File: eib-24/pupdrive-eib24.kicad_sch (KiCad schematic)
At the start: 27 parts, among them J1 050702422

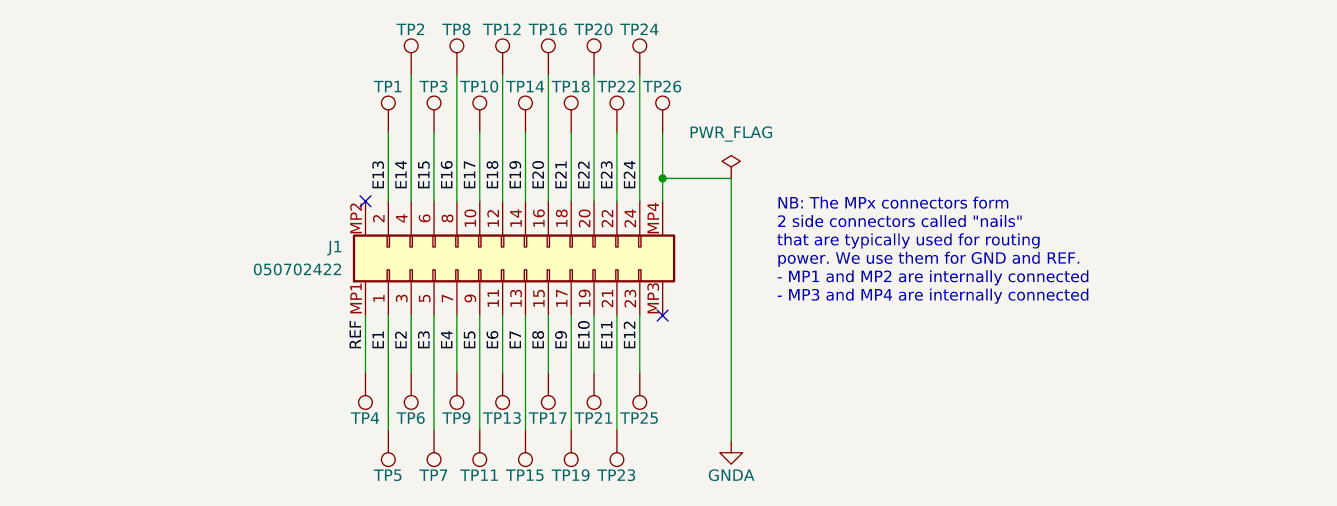
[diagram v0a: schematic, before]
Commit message: Make eib-24 smaller to fit leaf-spring drive
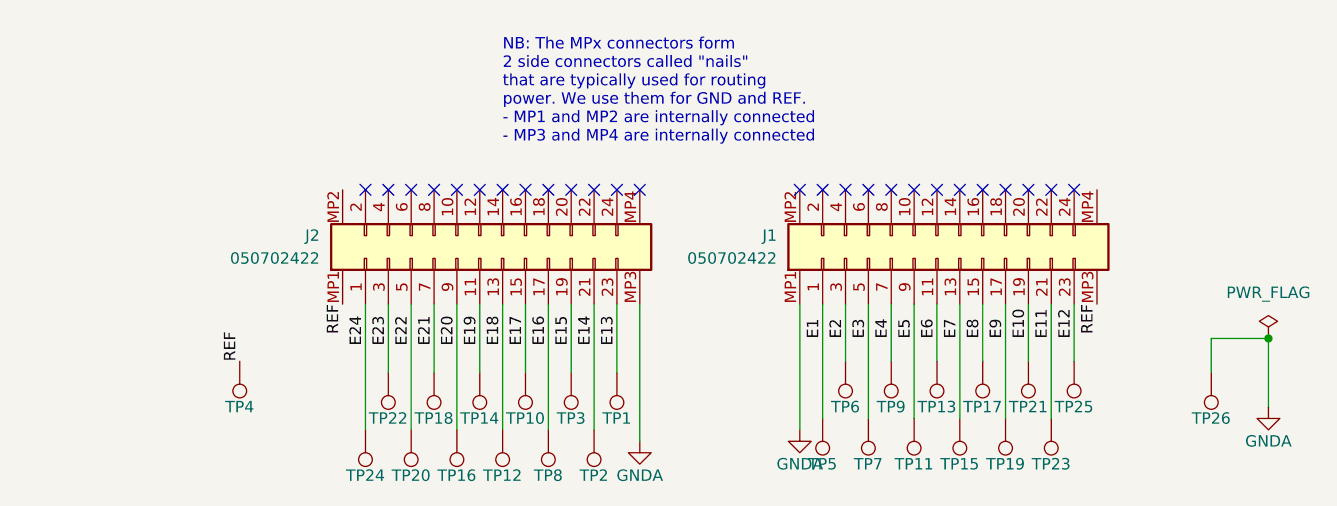
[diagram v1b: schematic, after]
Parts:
- added J2: 050702422, jonnew:MOLEX_5050702422, symbol jonnew:Conn_02x12_Odd_Even_4Mech
- TP26, TP4: footprint jonnew:NEURALYNX_LARGE-GOLD-PIN -> jonnew:NEURALYNX_SMALL-GOLD-PIN
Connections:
- net E13: now also J2.23 (Pin_23); no longer J1.2 (Pin_2)
- net E14: now also J2.21 (Pin_21); no longer J1.4 (Pin_4)
- net E15: now also J2.19 (Pin_19); no longer J1.6 (Pin_6)
- net E16: now also J2.17 (Pin_17); no longer J1.8 (Pin_8)
- net E17: now also J2.15 (Pin_15); no longer J1.10 (Pin_10)
- net E18: now also J2.13 (Pin_13); no longer J1.12 (Pin_12)
- net E19: now also J2.11 (Pin_11); no longer J1.14 (Pin_14)
- net E20: now also J2.9 (Pin_9); no longer J1.16 (Pin_16)
- net E21: now also J2.7 (Pin_7); no longer J1.18 (Pin_18)
- net E22: now also J2.5 (Pin_5); no longer J1.20 (Pin_20)
- net E23: now also J2.3 (Pin_3); no longer J1.22 (Pin_22)
- net E24: now also J2.1 (Pin_1); no longer J1.24 (Pin_24)
- net GNDA: now also J1.MP1 (MountPin1), J2.MP3 (MountPin3); no longer J1.MP4 (MountPin4)
- net REF: now also J1.MP3 (MountPin3), J2.MP1 (MountPin1); no longer J1.MP1 (MountPin1)
- no-connect marks 2 -> 26
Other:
- moved on the sheet: J1, TP1, TP10, TP11, TP12, TP13, TP14, TP15, TP16, TP17, TP18, TP19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

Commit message: Flex connector and eib-24 complete
- I need to panelize these and make different variants of the flex
connector with different lengths.
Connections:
- net GNDA: now also J1.MP3 (MountPin3), J2.MP1 (MountPin1); no longer J1.MP1 (MountPin1), J2.MP3 (MountPin3)
- net REF: now also J1.MP1 (MountPin1), J2.MP3 (MountPin3); no longer J1.MP3 (MountPin3), J2.MP1 (MountPin1)
- no-connect marks 26 -> 28
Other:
- moved on the sheet: J1, J2, TP1, TP10, TP11, TP12, TP13, TP14, TP15, TP16, TP17, TP18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
